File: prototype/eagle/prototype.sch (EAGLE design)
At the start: 41 parts, among them T1 3904, U1 ARDUINO_MINI_PRO, U2 ATA6631, U4 FTDI-BOARD

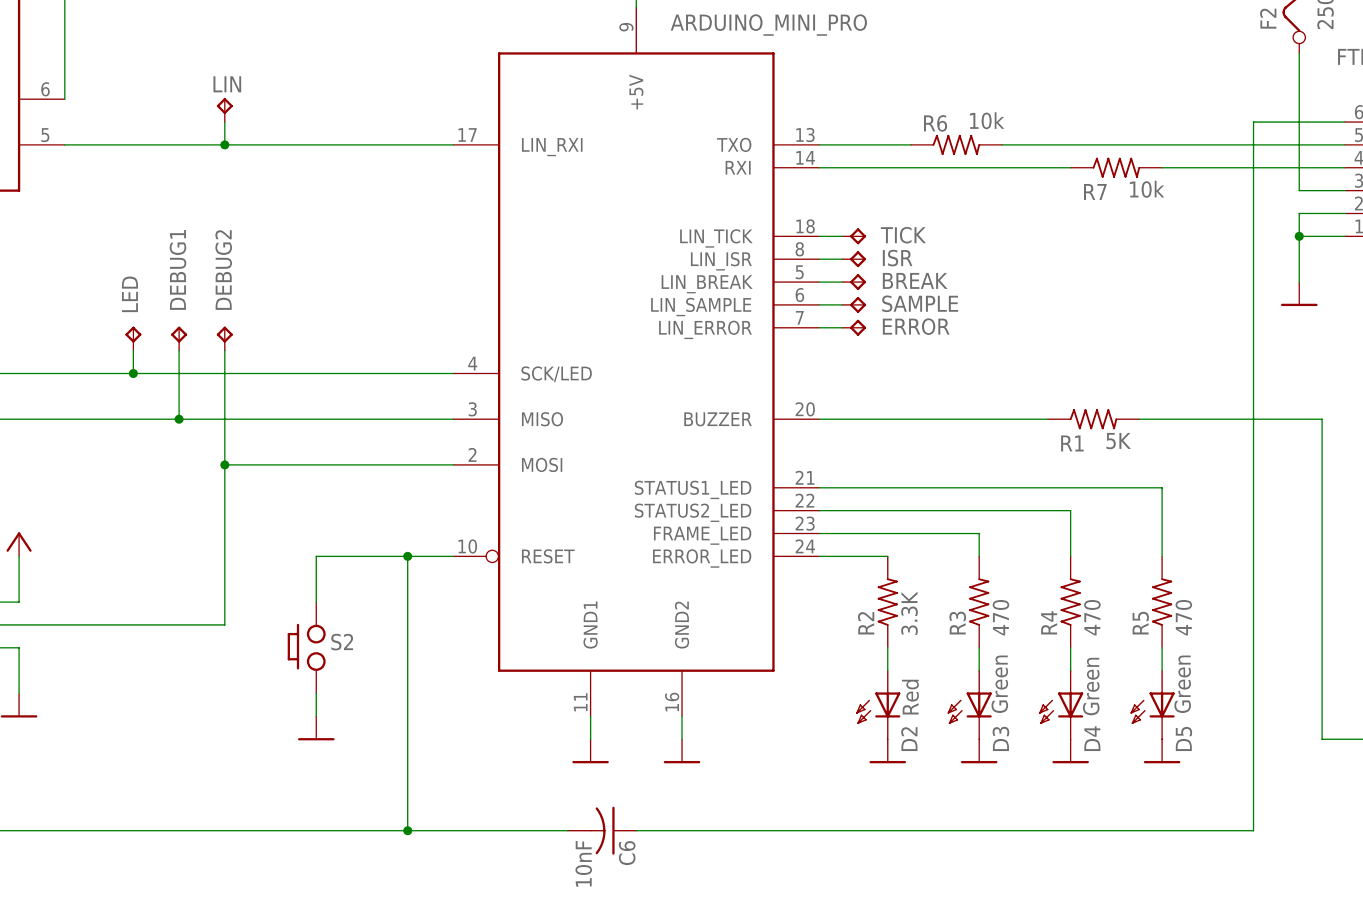
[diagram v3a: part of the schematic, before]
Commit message: Moved two debug pins to MISO/MOSI to free I/O pins.
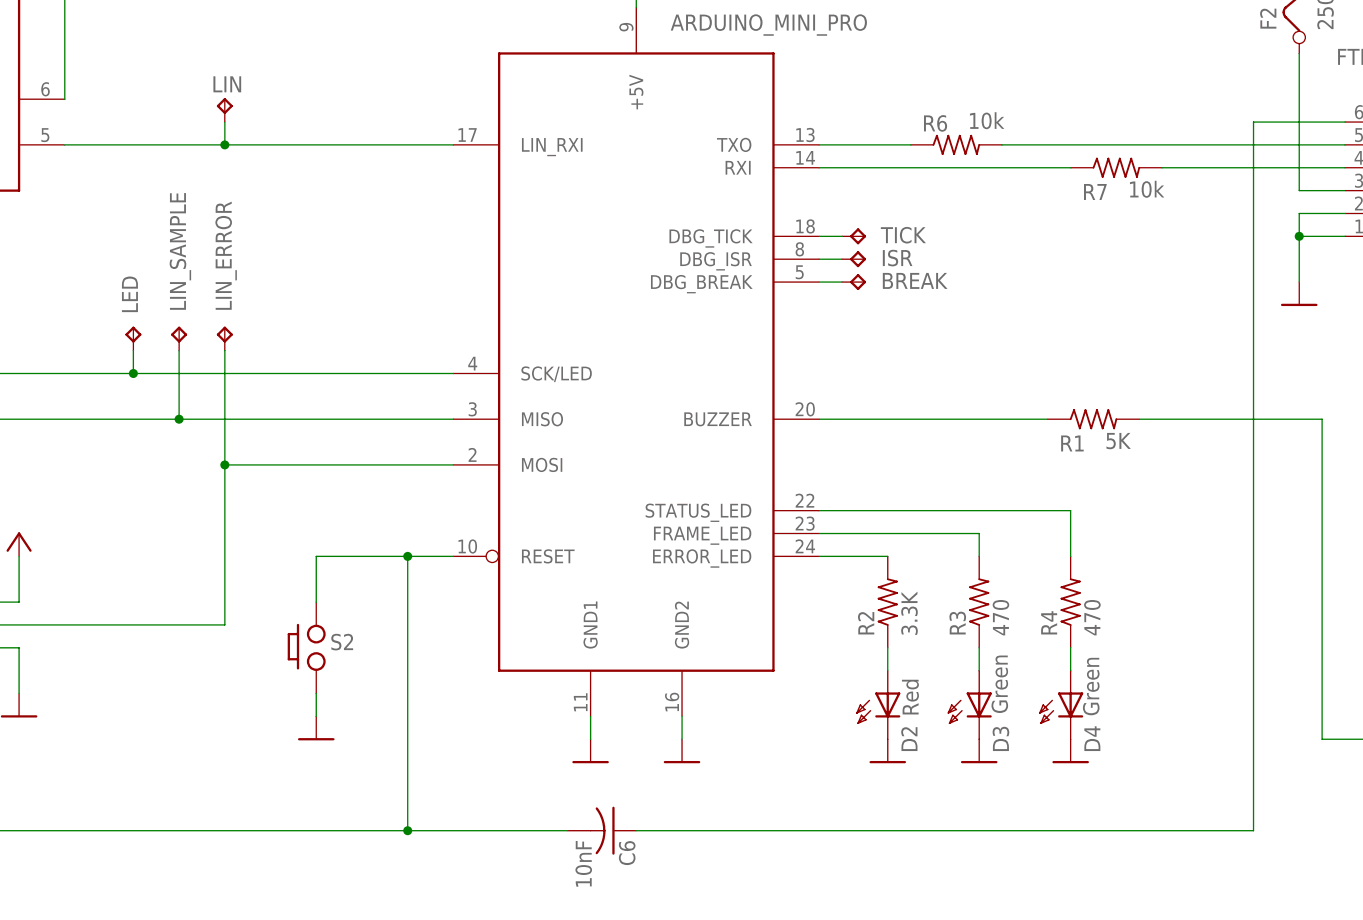
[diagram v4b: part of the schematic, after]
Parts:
- removed D5: Green, display-hp:HLMP6
- removed ERROR, SAMPLE: TPPAD1-17, testpad:TPPAD1-17
- removed R5: 470, rcl:R-US_R0805
- renumbered DEBUG1 to LIN_SAMPLE, DEBUG2 to LIN_ERROR
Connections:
- removed net N$1: D5.A, R5.1
- removed net N$10: R5.2, U1.STATUS1_LED
- removed net N$11: ERROR.TP, U1.LIN_ERROR
- removed net N$6: SAMPLE.TP, U1.LIN_SAMPLE
- net GND: no longer D5.K
- net N$26: now also U1.DBG_TICK; no longer U1.LIN_TICK
- net N$29: now also U1.DBG_ISR; no longer U1.LIN_ISR
- net N$5: now also U1.DBG_BREAK; no longer U1.LIN_BREAK
- net N$9: now also U1.STATUS_LED; no longer U1.STATUS2_LED
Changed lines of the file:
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@@
 <part name="R3" library="rcl" deviceset="R-US_" device="R0805" value="470"/>
 <part name="R4" library="rcl" deviceset="R-US_" device="R0805" value="470"/>
-<part name="R5" library="rcl" deviceset="R-US_" device="R0805" value="470"/>
 <part name="D2" library="display-hp" deviceset="HLMP6" device="" value="Red"/>
 <part name="D3" library="display-hp" deviceset="HLMP6" device="" value="Green"/>
 <part name="D4" library="display-hp" deviceset="HLMP6" device="" value="Green"/>
-<part name="D5" library="display-hp" deviceset="HLMP6" device="" value="Green"/>
 <part name="S2" library="prototype" deviceset="PUSH_BUTTON" device=""/>
 <part name="C1" library="rcl" deviceset="C-US" device="C0805" value="0.1uF 40V"/>
@@
 <part name="GND2" library="prototype" deviceset="GND" device=""/>
 <part name="GND13" library="prototype" deviceset="GND" device=""/>
-<part name="GND15" library="prototype" deviceset="GND" device=""/>
 <part name="BREAK" library="testpad" deviceset="TP" device="PAD1-17"/>
-<part name="SAMPLE" library="testpad" deviceset="TP" device="PAD1-17"/>
-<part name="ERROR" library="testpad" deviceset="TP" device="PAD1-17"/>
 <part name="GND16" library="prototype" deviceset="GND" device=""/>
 <part name="F2" library="special" deviceset="FUSE" device="" value="250ma Slow"/>
@@
 <part name="GND14" library="prototype" deviceset="GND" device=""/>
 <part name="P+5" library="supply1" deviceset="+5V" device=""/>
-<part name="DEBUG1" library="testpad" deviceset="TP" device="PAD1-17"/>
-<part name="DEBUG2" library="testpad" deviceset="TP" device="PAD1-17"/>
+<part name="LIN_SAMPLE" library="testpad" deviceset="TP" device="PAD1-17"/>
+<part name="LIN_ERROR" library="testpad" deviceset="TP" device="PAD1-17"/>
 <part name="ISR" library="testpad" deviceset="TP" device="PAD1-17"/>
 <part name="SG1" library="buzzer" deviceset="F/SMX" device="" value=""/>
@@
 <instance part="R3" gate="G$1" x="238.76" y="96.52" rot="R90"/>
 <instance part="R4" gate="G$1" x="248.92" y="96.52" rot="R90"/>
-<instance part="R5" gate="G$1" x="259.08" y="96.52" rot="R90"/>
 <instance part="D2" gate="A" x="228.6" y="83.82" smashed="yes">
 <attribute name="NAME" x="231.902" y="79.756" size="1.778" layer="95" rot="R90"/>
@@
 <attribute name="NAME" x="252.222" y="79.756" size="1.778" layer="95" rot="R90"/>
 <attribute name="VALUE" x="252.095" y="83.82" size="1.778" layer="96" rot="R90"/>
-</instance>
-<instance part="D5" gate="A" x="259.08" y="83.82" smashed="yes">
-<attribute name="NAME" x="262.382" y="79.756" size="1.778" layer="95" rot="R90"/>
-<attribute name="VALUE" x="262.255" y="84.074" size="1.778" layer="96" rot="R90"/>
 </instance>
 <instance part="S2" gate="G$1" x="165.1" y="91.44"/>
@@
 <instance part="GND2" gate="1" x="238.76" y="78.74"/>
 <instance part="GND13" gate="1" x="248.92" y="78.74"/>
-<instance part="GND15" gate="1" x="259.08" y="78.74"/>
 <instance part="BREAK" gate="G$1" x="226.06" y="132.08" smashed="yes" rot="R270">
 <attribute name="NAME" x="227.838" y="131.318" size="1.778" layer="95"/>
 <attribute name="TP_SIGNAL_NAME" x="224.79" y="130.81" size="1.778" layer="97" rot="R270"/>
-</instance>
-<instance part="SAMPLE" gate="G$1" x="226.06" y="129.54" smashed="yes" rot="R270">
-<attribute name="NAME" x="227.838" y="128.778" size="1.778" layer="95"/>
-<attribute name="TP_SIGNAL_NAME" x="224.79" y="128.27" size="1.778" layer="97" rot="R270"/>
-</instance>
-<instance part="ERROR" gate="G$1" x="226.06" y="127" smashed="yes" rot="R270">
-<attribute name="NAME" x="227.838" y="126.238" size="1.778" layer="95"/>
-<attribute name="TP_SIGNAL_NAME" x="224.79" y="125.73" size="1.778" layer="97" rot="R270"/>
 </instance>
 <instance part="GND16" gate="1" x="205.74" y="78.74"/>
@@
 <attribute name="VALUE" x="129.54" y="100.838" size="1.778" layer="96" rot="R90"/>
 </instance>
-<instance part="DEBUG1" gate="G$1" x="149.86" y="127" smashed="yes">
+<instance part="LIN_SAMPLE" gate="G$1" x="149.86" y="127" smashed="yes">
 <attribute name="NAME" x="150.622" y="128.778" size="1.778" layer="95" rot="R90"/>
 <attribute name="TP_SIGNAL_NAME" x="151.13" y="125.73" size="1.778" layer="97"/>
 </instance>
-<instance part="DEBUG2" gate="G$1" x="154.94" y="127" smashed="yes">
+<instance part="LIN_ERROR" gate="G$1" x="154.94" y="127" smashed="yes">
 <attribute name="NAME" x="155.702" y="128.778" size="1.778" layer="95" rot="R90"/>
 <attribute name="TP_SIGNAL_NAME" x="156.21" y="125.73" size="1.778" layer="97"/>
@@
 </segment>
 <segment>
-<pinref part="D5" gate="A" pin="K"/>
-<pinref part="GND15" gate="1" pin="GND"/>
-</segment>
-<segment>
 <pinref part="D3" gate="A" pin="K"/>
 <pinref part="GND2" gate="1" pin="GND"/>
@@
 <pinref part="C5" gate="G$1" pin="-"/>
 <pinref part="GND11" gate="1" pin="GND"/>
-</segment>
-</net>
-<net name="N$1" class="0">
-<segment>
-<pinref part="R5" gate="G$1" pin="1"/>
-<pinref part="D5" gate="A" pin="A"/>
-<wire x1="259.08" y1="91.44" x2="259.08" y2="88.9" width="0.1524" layer="91"/>
 </segment>
 </net>
@@
 <net name="N$26" class="0">
 <segment>
-<pinref part="U1" gate="G$1" pin="LIN_TICK"/>
+<pinref part="U1" gate="G$1" pin="DBG_TICK"/>
 <pinref part="TICK" gate="G$1" pin="TP"/>
 <wire x1="223.52" y1="137.16" x2="220.98" y2="137.16" width="0.1524" layer="91"/>
@@
 <net name="N$5" class="0">
 <segment>
-<pinref part="U1" gate="G$1" pin="LIN_BREAK"/>
+<pinref part="U1" gate="G$1" pin="DBG_BREAK"/>
 <pinref part="BREAK" gate="G$1" pin="TP"/>
 <wire x1="220.98" y1="132.08" x2="223.52" y2="132.08" width="0.1524" layer="91"/>
-</segment>
-</net>
-<net name="N$6" class="0">
-<segment>
-<pinref part="U1" gate="G$1" pin="LIN_SAMPLE"/>
-<pinref part="SAMPLE" gate="G$1" pin="TP"/>
-<wire x1="220.98" y1="129.54" x2="223.52" y2="129.54" width="0.1524" layer="91"/>
-</segment>
-</net>
-<net name="N$11" class="0">
-<segment>
-<pinref part="U1" gate="G$1" pin="LIN_ERROR"/>
-<pinref part="ERROR" gate="G$1" pin="TP"/>
-<wire x1="220.98" y1="127" x2="223.52" y2="127" width="0.1524" layer="91"/>
 </segment>
 </net>
@@
 <wire x1="154.94" y1="111.76" x2="180.34" y2="111.76" width="0.1524" layer="91"/>
 <pinref part="U1" gate="G$1" pin="MOSI"/>
-<pinref part="DEBUG2" gate="G$1" pin="TP"/>
+<pinref part="LIN_ERROR" gate="G$1" pin="TP"/>
 <wire x1="154.94" y1="124.46" x2="154.94" y2="111.76" width="0.1524" layer="91"/>
 <junction x="154.94" y="111.76"/>
@@
 <pinref part="U1" gate="G$1" pin="MISO"/>
 <wire x1="149.86" y1="116.84" x2="180.34" y2="116.84" width="0.1524" layer="91"/>
-<pinref part="DEBUG1" gate="G$1" pin="TP"/>
+<pinref part="LIN_SAMPLE" gate="G$1" pin="TP"/>
 <wire x1="149.86" y1="124.46" x2="149.86" y2="116.84" width="0.1524" layer="91"/>
 <junction x="149.86" y="116.84"/>
@@
 <net name="N$9" class="0">
 <segment>
-<pinref part="U1" gate="G$1" pin="STATUS2_LED"/>
+<pinref part="U1" gate="G$1" pin="STATUS_LED"/>
 <pinref part="R4" gate="G$1" pin="2"/>
 <wire x1="220.98" y1="106.68" x2="248.92" y2="106.68" width="0.1524" layer="91"/>
@@
 </segment>
 </net>
-<net name="N$10" class="0">
-<segment>
-<pinref part="U1" gate="G$1" pin="STATUS1_LED"/>
-<pinref part="R5" gate="G$1" pin="2"/>
-<wire x1="220.98" y1="109.22" x2="259.08" y2="109.22" width="0.1524" layer="91"/>
-<wire x1="259.08" y1="109.22" x2="259.08" y2="101.6" width="0.1524" layer="91"/>
-</segment>
-</net>
 <net name="N$29" class="0">
 <segment>
-<pinref part="U1" gate="G$1" pin="LIN_ISR"/>
+<pinref part="U1" gate="G$1" pin="DBG_ISR"/>
 <pinref part="ISR" gate="G$1" pin="TP"/>
 <wire x1="220.98" y1="134.62" x2="223.52" y2="134.62" width="0.1524" layer="91"/>

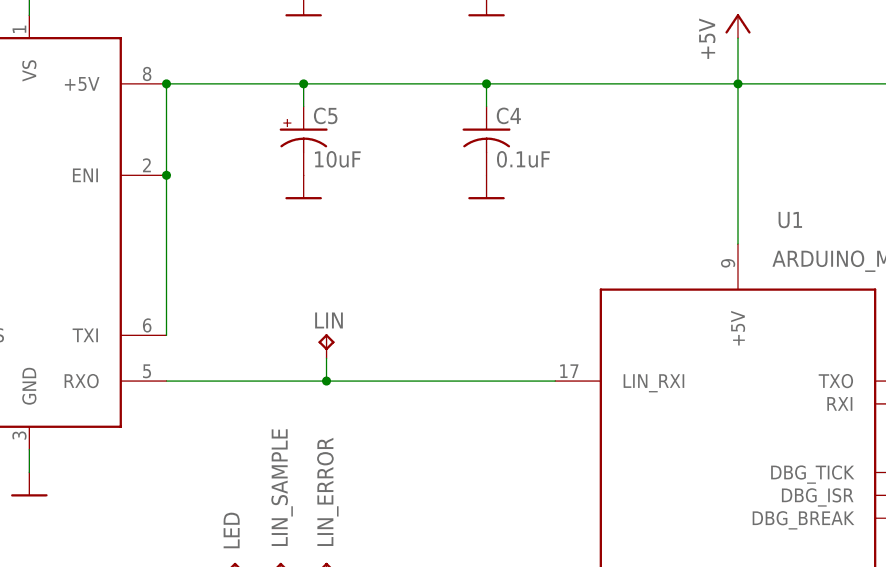
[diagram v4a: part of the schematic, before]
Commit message: Prototype can now transmit to the linbus. Software not implemented yet.
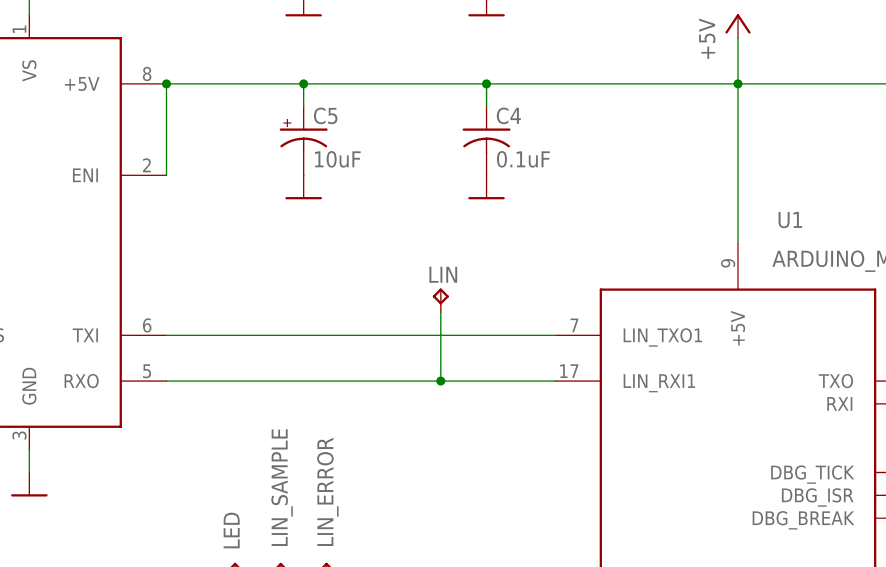
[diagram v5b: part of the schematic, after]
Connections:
- new net N$1: U1.LIN_TXO1, U2.TXI
- net +5V: no longer U2.TXI
- net N$18: now also U1.LIN_RXI1; no longer U1.LIN_RXI
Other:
- moved on the sheet: LIN
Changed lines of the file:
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@@
 <attribute name="TP_SIGNAL_NAME" x="146.05" y="125.73" size="1.778" layer="97"/>
 </instance>
-<instance part="LIN" gate="G$1" x="154.94" y="152.4" smashed="yes">
-<attribute name="NAME" x="156.972" y="154.94" size="1.778" layer="95" rot="R180"/>
-<attribute name="TP_SIGNAL_NAME" x="156.21" y="151.13" size="1.778" layer="97"/>
+<instance part="LIN" gate="G$1" x="167.64" y="157.48" smashed="yes">
+<attribute name="NAME" x="169.672" y="160.02" size="1.778" layer="95" rot="R180"/>
+<attribute name="TP_SIGNAL_NAME" x="168.91" y="156.21" size="1.778" layer="97"/>
 </instance>
 <instance part="GND2" gate="1" x="238.76" y="78.74"/>
@@
 <net name="N$18" class="0">
 <segment>
-<wire x1="180.34" y1="147.32" x2="154.94" y2="147.32" width="0.1524" layer="91"/>
-<pinref part="U1" gate="G$1" pin="LIN_RXI"/>
+<wire x1="180.34" y1="147.32" x2="167.64" y2="147.32" width="0.1524" layer="91"/>
+<pinref part="U1" gate="G$1" pin="LIN_RXI1"/>
 <pinref part="LIN" gate="G$1" pin="TP"/>
-<wire x1="137.16" y1="147.32" x2="154.94" y2="147.32" width="0.1524" layer="91"/>
-<wire x1="154.94" y1="149.86" x2="154.94" y2="147.32" width="0.1524" layer="91"/>
-<junction x="154.94" y="147.32"/>
+<wire x1="137.16" y1="147.32" x2="167.64" y2="147.32" width="0.1524" layer="91"/>
+<wire x1="167.64" y1="154.94" x2="167.64" y2="147.32" width="0.1524" layer="91"/>
+<junction x="167.64" y="147.32"/>
 <pinref part="U2" gate="G$1" pin="RXO"/>
 </segment>
@@
 <junction x="152.4" y="180.34"/>
 <junction x="172.72" y="180.34"/>
-<pinref part="U2" gate="G$1" pin="TXI"/>
-<wire x1="137.16" y1="152.4" x2="137.16" y2="170.18" width="0.1524" layer="91"/>
 <pinref part="U2" gate="G$1" pin="ENI"/>
 <wire x1="137.16" y1="170.18" x2="137.16" y2="180.34" width="0.1524" layer="91"/>
-<junction x="137.16" y="170.18"/>
 <junction x="137.16" y="180.34"/>
 </segment>
@@
 </segment>
 </net>
+<net name="N$1" class="0">
+<segment>
+<pinref part="U2" gate="G$1" pin="TXI"/>
+<pinref part="U1" gate="G$1" pin="LIN_TXO1"/>
+<wire x1="137.16" y1="152.4" x2="180.34" y2="152.4" width="0.1524" layer="91"/>
+</segment>
+</net>
